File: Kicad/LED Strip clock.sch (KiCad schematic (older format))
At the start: 81 parts, among them J1 Conn_01x09_Male, J2 Conn_01x09_Male, J3 Conn_01x09_Male, J4 Conn_01x09_Male, J5 Conn_01x04_Male, J6 Barrel_Jack_Switch, U1 TPIC6B595, U10 5611BH, U11 5611BH, U12 5611BH, U13 MCP23008-xSO, U14 INA219AxDCN, U2 TPIC6B595, U3 TPIC6B595, U4 TPIC6B595, U5 74HCT244, U6 WeMos_D1_mini, U7 MAX809S, U8 L7805, U9 5611BH

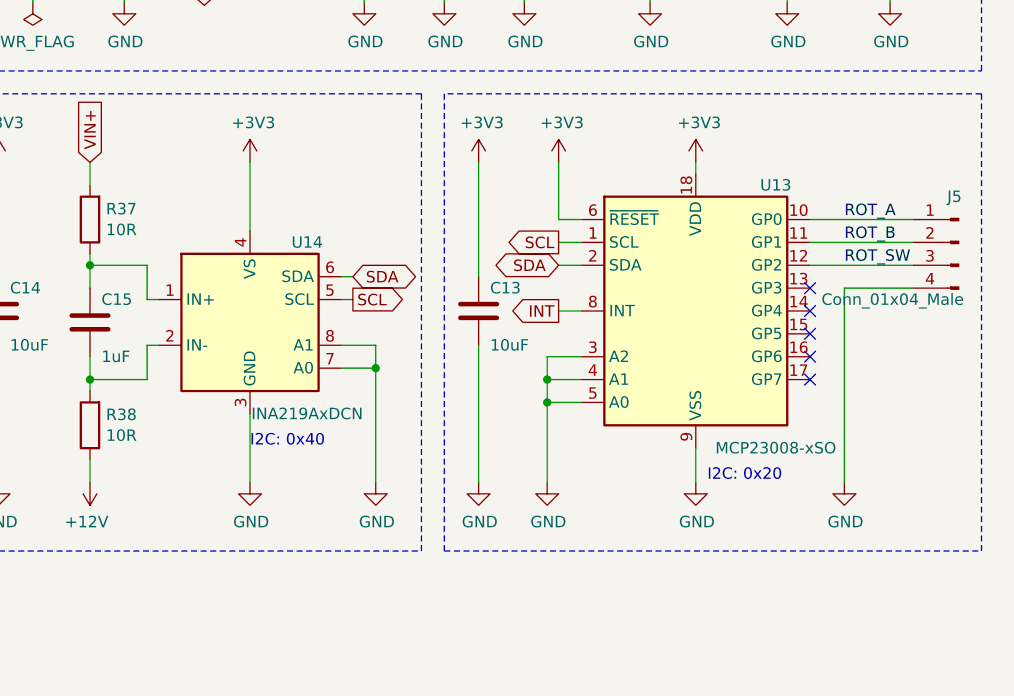
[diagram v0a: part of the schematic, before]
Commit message: Changed INA219AxDCN to INA219AxD.
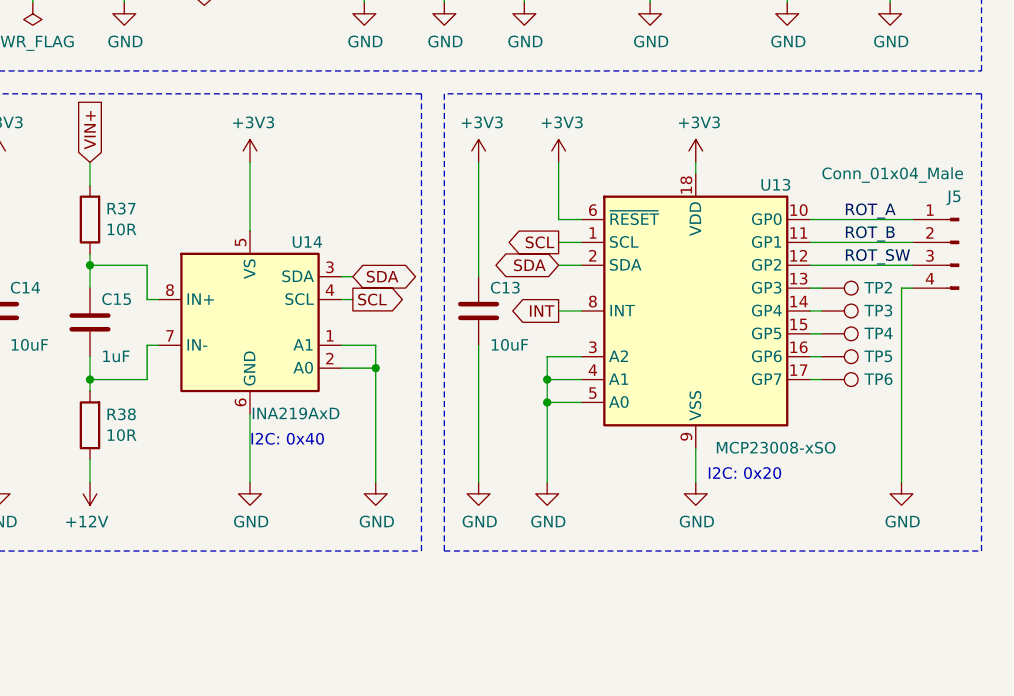
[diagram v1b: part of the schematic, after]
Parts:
- removed U14: INA219AxDCN, Package_TO_SOT_SMD:SOT-23-8, symbol Analog_ADC:INA219AxDCN
- added TP2, TP3, TP4, TP5, TP6: TestPoint, TestPoint:TestPoint_Pad_D1.0mm, symbol Connector:TestPoint
- added U14: INA219AxD, Package_SO:SOIC-8_3.9x4.9mm_P1.27mm, symbol Analog_ADC:INA219AxD
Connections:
- net +3V3: now also U14.5 (VS)
- net GND: now also U14.1 (A1), U14.2 (A0), U14.6 (GND)
- net SCL: now also U14.4 (SCL)
- net SDA: now also U14.3 (SDA)
- net at U13.13 (GP3): now also TP2.1
- net at U13.14 (GP4): now also TP3.1
- net at U13.15 (GP5): now also TP4.1
- net at U13.16 (GP6): now also TP5.1
- net at U13.17 (GP7): now also TP6.1
- net at C15.1, R37.1: now also U14.8 (IN+)
- net at C15.2, R38.2: now also U14.7 (IN-)
- no-connect marks 12 -> 7
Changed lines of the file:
@@
 Sheet 1 1
 Title "Driver for LED Strip clock"
-Date "2021-05-04"
+Date "2021-08-06"
 Rev "V1.0"
 Comp "https://github.com/atoomnetmarc/LED-Strip-clock"
@@
 P 11050 5100
 F 0 "J5" H 11100 5300 50  0000 R CNN
-F 1 "Conn_01x04_Male" H 11650 4850 50  0000 R CNN
+F 1 "Conn_01x04_Male" H 11650 5400 50  0000 R CNN
 F 2 "Connector_PinHeader_2.54mm:PinHeader_1x04_P2.54mm_Vertical" H 11050 5100 50  0001 C CNN
 F 3 "~" H 11050 5100 50  0001 C CNN
@@
 L power:GND #PWR038
 U 1 1 6093ED9B
-P 10550 6150
-F 0 "#PWR038" H 10550 5900 50  0001 C CNN
-F 1 "GND" H 10555 5977 50  0000 C CNN
-F 2 "" H 10550 6150 50  0001 C CNN
-F 3 "" H 10550 6150 50  0001 C CNN
-	1    10550 6150
+P 10800 6150
+F 0 "#PWR038" H 10800 5900 50  0001 C CNN
+F 1 "GND" H 10805 5977 50  0000 C CNN
+F 2 "" H 10800 6150 50  0001 C CNN
+F 3 "" H 10800 6150 50  0001 C CNN
+	1    10800 6150
 	1    0    0    -1
 $EndComp
@@
 ROT_SW
 Wire Wire Line
-	10550 5300 10550 6150
-Wire Wire Line
-	10550 5300 10850 5300
+	10800 5300 10800 6150
+Wire Wire Line
+	10800 5300 10850 5300
 Text Label 5250 3550 0    50   ~ 0
 ~OE_5V
@@
 Wire Wire Line
 	10400 5200 10850 5200
-NoConn ~ 10400 5300
-NoConn ~ 10400 5400
-NoConn ~ 10400 5500
-NoConn ~ 10400 5600
-NoConn ~ 10400 5700
 $Comp
 L power:GND #PWR060
@@
 Wire Notes Line
 	8700 6450 8700 4450
-$Comp
-L Analog_ADC:INA219AxDCN U14
-U 1 1 6147942B
-P 7950 5450
-F 0 "U14" H 8200 5800 50  0000 C CNN
-F 1 "INA219AxDCN" H 8200 5050 50  0000 C CNN
-F 2 "Package_TO_SOT_SMD:SOT-23-8" H 8600 5100 50  0001 C CNN
-F 3 "http://www.ti.com/lit/ds/symlink/ina219.pdf" H 8300 5350 50  0001 C CNN
-	1    7950 5450
-	1    0    0    -1
-$EndComp
 Text GLabel 8400 5250 2    50   BiDi ~ 0
 SDA
@@
 	-1   0    0    1
 $EndComp
+$Comp
+L Analog_ADC:INA219AxD U14
+U 1 1 610F2B75
+P 7950 5450
+F 0 "U14" H 8200 5800 50  0000 C CNN
+F 1 "INA219AxD" H 8150 5050 50  0000 C CNN
+F 2 "Package_SO:SOIC-8_3.9x4.9mm_P1.27mm" H 8750 5100 50  0001 C CNN
+F 3 "http://www.ti.com/lit/ds/symlink/ina219.pdf" H 8300 5350 50  0001 C CNN
+	1    7950 5450
+	1    0    0    -1
+$EndComp
+$Comp
+L Connector:TestPoint TP2
+U 1 1 611BBE01
+P 10450 5300
+F 0 "TP2" V 10450 5488 50  0000 L CNN
+F 1 "TestPoint" V 10495 5488 50  0001 L CNN
+F 2 "TestPoint:TestPoint_Pad_D1.0mm" H 10650 5300 50  0001 C CNN
+F 3 "~" H 10650 5300 50  0001 C CNN
+	1    10450 5300
+	0    1    1    0
+$EndComp
+$Comp
+L Connector:TestPoint TP3
+U 1 1 611BCA6F
+P 10450 5400
+F 0 "TP3" V 10450 5588 50  0000 L CNN
+F 1 "TestPoint" V 10495 5588 50  0001 L CNN
+F 2 "TestPoint:TestPoint_Pad_D1.0mm" H 10650 5400 50  0001 C CNN
+F 3 "~" H 10650 5400 50  0001 C CNN
+	1    10450 5400
+	0    1    1    0
+$EndComp
+$Comp
+L Connector:TestPoint TP4
+U 1 1 611BCC45
+P 10450 5500
+F 0 "TP4" V 10450 5688 50  0000 L CNN
+F 1 "TestPoint" V 10495 5688 50  0001 L CNN
+F 2 "TestPoint:TestPoint_Pad_D1.0mm" H 10650 5500 50  0001 C CNN
+F 3 "~" H 10650 5500 50  0001 C CNN
+	1    10450 5500
+	0    1    1    0
+$EndComp
+$Comp
+L Connector:TestPoint TP5
+U 1 1 611BCDDE
+P 10450 5600
+F 0 "TP5" V 10450 5788 50  0000 L CNN
+F 1 "TestPoint" V 10495 5788 50  0001 L CNN
+F 2 "TestPoint:TestPoint_Pad_D1.0mm" H 10650 5600 50  0001 C CNN
+F 3 "~" H 10650 5600 50  0001 C CNN
+	1    10450 5600
+	0    1    1    0
+$EndComp
+$Comp
+L Connector:TestPoint TP6
+U 1 1 611BCFF7
+P 10450 5700
+F 0 "TP6" V 10450 5888 50  0000 L CNN
+F 1 "TestPoint" V 10495 5888 50  0001 L CNN
+F 2 "TestPoint:TestPoint_Pad_D1.0mm" H 10650 5700 50  0001 C CNN
+F 3 "~" H 10650 5700 50  0001 C CNN
+	1    10450 5700
+	0    1    1    0
+$EndComp
+Wire Wire Line
+	10400 5300 10450 5300
+Wire Wire Line
+	10450 5400 10400 5400
+Wire Wire Line
+	10400 5500 10450 5500
+Wire Wire Line
+	10450 5600 10400 5600
+Wire Wire Line
+	10400 5700 10450 5700
 $EndSCHEMATC

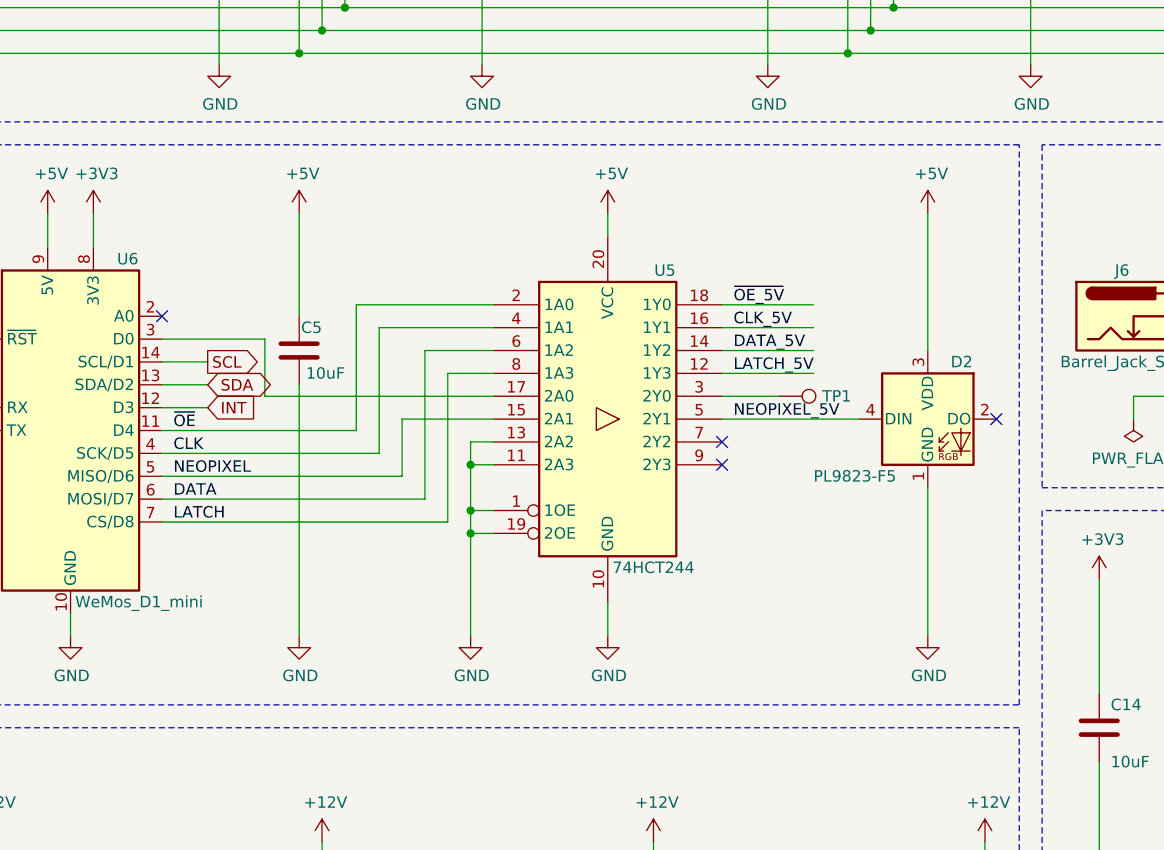
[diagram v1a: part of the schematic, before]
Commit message: Fixed power-on flash of digits.
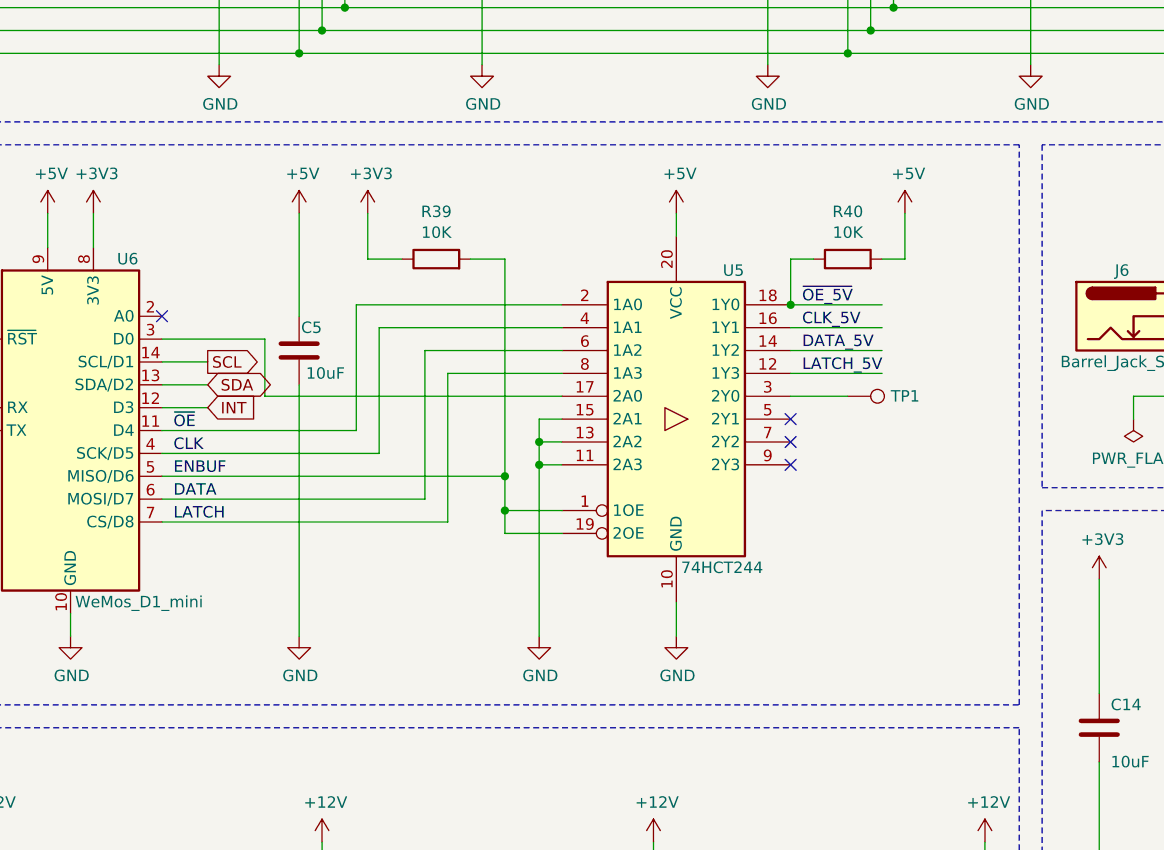
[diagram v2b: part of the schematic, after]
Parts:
- removed D2: PL9823-F5, LED_THT-extra:LED_D5.0mm-4_PL9823-F5, symbol LED-extra:PL9823-F5
- added R39, R40: 10K, Resistor_SMD:R_0805_2012Metric_Pad1.20x1.40mm_HandSolder, symbol Device:R
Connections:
- net +3V3: now also R39.1
- net +5V: now also R40.2
- net GND: now also U5.15 (2A1); no longer U5.1 (1OE), U5.19 (2OE)
- net ~OE_5V: now also R40.1
- net NEOPIXEL renamed ENBUF
- net ENBUF: now also U5.1 (1OE), U5.19 (2OE), R39.2; no longer U5.15 (2A1)
- net NEOPIXEL_5V: no longer names the net of U5.5 (2Y1)
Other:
- moved on the sheet: TP1, U5
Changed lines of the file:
@@
 Sheet 1 1
 Title "Driver for LED Strip clock"
-Date "2021-08-06"
+Date "2021-08-30"
 Rev "V1.0"
 Comp "https://github.com/atoomnetmarc/LED-Strip-clock"
@@
 L 74xx:74HCT244 U5
 U 1 1 608C7AB1
-P 4700 4050
-F 0 "U5" H 4950 4700 50  0000 C CNN
-F 1 "74HCT244" H 4900 3400 50  0000 C CNN
-F 2 "Package_DIP:DIP-20_W7.62mm_LongPads" H 4700 4050 50  0001 C CNN
-F 3 "https://assets.nexperia.com/documents/data-sheet/74HC_HCT244.pdf" H 4700 4050 50  0001 C CNN
-	1    4700 4050
+P 5000 4050
+F 0 "U5" H 5250 4700 50  0000 C CNN
+F 1 "74HCT244" H 5200 3400 50  0000 C CNN
+F 2 "Package_DIP:DIP-20_W7.62mm_LongPads" H 5000 4050 50  0001 C CNN
+F 3 "https://assets.nexperia.com/documents/data-sheet/74HC_HCT244.pdf" H 5000 4050 50  0001 C CNN
+	1    5000 4050
 	1    0    0    -1
 $EndComp
@@
 L power:GND #PWR041
 U 1 1 608CF759
-P 4700 5000
-F 0 "#PWR041" H 4700 4750 50  0001 C CNN
-F 1 "GND" H 4705 4827 50  0000 C CNN
-F 2 "" H 4700 5000 50  0001 C CNN
-F 3 "" H 4700 5000 50  0001 C CNN
-	1    4700 5000
+P 5000 5000
+F 0 "#PWR041" H 5000 4750 50  0001 C CNN
+F 1 "GND" H 5005 4827 50  0000 C CNN
+F 2 "" H 5000 5000 50  0001 C CNN
+F 3 "" H 5000 5000 50  0001 C CNN
+	1    5000 5000
 	1    0    0    -1
 $EndComp
@@
 L power:GND #PWR040
 U 1 1 608D1492
-P 4100 5000
-F 0 "#PWR040" H 4100 4750 50  0001 C CNN
-F 1 "GND" H 4105 4827 50  0000 C CNN
-F 2 "" H 4100 5000 50  0001 C CNN
-F 3 "" H 4100 5000 50  0001 C CNN
-	1    4100 5000
-	1    0    0    -1
-$EndComp
-Wire Wire Line
-	4200 4550 4100 4550
-Wire Wire Line
-	4100 4550 4100 5000
-Wire Wire Line
-	4200 4450 4100 4450
-Wire Wire Line
-	4100 4450 4100 4550
-Connection ~ 4100 4550
-Wire Wire Line
-	4700 4850 4700 5000
-Wire Wire Line
-	5200 3750 5600 3750
-Wire Wire Line
-	5200 3650 5600 3650
+P 4400 5000
+F 0 "#PWR040" H 4400 4750 50  0001 C CNN
+F 1 "GND" H 4405 4827 50  0000 C CNN
+F 2 "" H 4400 5000 50  0001 C CNN
+F 3 "" H 4400 5000 50  0001 C CNN
+	1    4400 5000
+	1    0    0    -1
+$EndComp
+Wire Wire Line
+	5000 4850 5000 5000
+Wire Wire Line
+	5500 3750 5900 3750
+Wire Wire Line
+	5500 3650 5900 3650
 $Comp
 L power:+5V #PWR031
 U 1 1 608D4D74
-P 4700 3150
-F 0 "#PWR031" H 4700 3000 50  0001 C CNN
-F 1 "+5V" H 4715 3323 50  0000 C CNN
-F 2 "" H 4700 3150 50  0001 C CNN
-F 3 "" H 4700 3150 50  0001 C CNN
-	1    4700 3150
-	1    0    0    -1
-$EndComp
-Wire Wire Line
-	4700 3250 4700 3150
-Wire Wire Line
-	5200 3850 5600 3850
-Wire Wire Line
-	5200 3550 5600 3550
-Wire Wire Line
-	4000 3850 4200 3850
-Wire Wire Line
-	3900 3750 4200 3750
-Wire Wire Line
-	3700 3650 4200 3650
-Wire Wire Line
-	3600 3550 4200 3550
+P 5000 3150
+F 0 "#PWR031" H 5000 3000 50  0001 C CNN
+F 1 "+5V" H 5015 3323 50  0000 C CNN
+F 2 "" H 5000 3150 50  0001 C CNN
+F 3 "" H 5000 3150 50  0001 C CNN
+	1    5000 3150
+	1    0    0    -1
+$EndComp
+Wire Wire Line
+	5000 3250 5000 3150
+Wire Wire Line
+	5500 3850 5900 3850
+Wire Wire Line
+	5500 3550 5900 3550
+Wire Wire Line
+	4000 3850 4500 3850
+Wire Wire Line
+	3900 3750 4500 3750
+Wire Wire Line
+	3700 3650 4500 3650
+Wire Wire Line
+	3600 3550 4500 3550
 $Comp
 L Connector:Conn_01x04_Male J5
@@
 Wire Wire Line
 	10800 5300 10850 5300
-Text Label 5250 3550 0    50   ~ 0
+Text Label 5550 3550 0    50   ~ 0
 ~OE_5V
-Text Label 5250 3850 0    50   ~ 0
+Text Label 5550 3850 0    50   ~ 0
 LATCH_5V
-Text Label 5250 3650 0    50   ~ 0
+Text Label 5550 3650 0    50   ~ 0
 CLK_5V
-Text Label 5250 3750 0    50   ~ 0
+Text Label 5550 3750 0    50   ~ 0
 DATA_5V
 $Comp
@@
 Wire Wire Line
 	3600 3550 3600 4100
-NoConn ~ 5200 4150
-NoConn ~ 5200 4250
-Wire Wire Line
-	4100 4450 4100 4250
-Wire Wire Line
-	4100 4250 4200 4250
-Connection ~ 4100 4450
-Wire Wire Line
-	4100 4250 4100 4150
-Wire Wire Line
-	4100 4150 4200 4150
-Connection ~ 4100 4250
+NoConn ~ 5500 4150
+NoConn ~ 5500 4250
+Wire Wire Line
+	4400 4250 4500 4250
+Wire Wire Line
+	4400 4250 4400 4150
+Wire Wire Line
+	4400 4150 4500 4150
+Connection ~ 4400 4250
 Wire Wire Line
 	10750 3500 10750 3150
@@
 $EndComp
 Wire Wire Line
-	3800 4300 3800 4050
-Wire Wire Line
-	3800 4050 4200 4050
-Wire Wire Line
-	4200 3950 3200 3950
+	4500 3950 3200 3950
 Wire Wire Line
 	3200 3950 3200 3700
@@
 L Connector:TestPoint TP1
 U 1 1 611FE123
-P 5450 3950
-F 0 "TP1" V 5450 4138 50  0000 L CNN
-F 1 "TestPoint" V 5495 4138 50  0001 L CNN
-F 2 "TestPoint:TestPoint_THTPad_D1.5mm_Drill0.7mm" H 5650 3950 50  0001 C CNN
-F 3 "~" H 5650 3950 50  0001 C CNN
-	1    5450 3950
-	0    1    1    0
-$EndComp
-Wire Wire Line
-	5200 3950 5450 3950
-$Comp
-L LED-extra:PL9823-F5 D2
-U 1 1 61220BB0
-P 6100 4050
-F 0 "D2" H 6200 4300 50  0000 L CNN
-F 1 "PL9823-F5" H 5600 3800 50  0000 L CNN
-F 2 "LED_THT-extra:LED_D5.0mm-4_PL9823-F5" H 6150 3750 50  0001 L TNN
-F 3 "" H 6200 3675 50  0001 L TNN
-	1    6100 4050
-	1    0    0    -1
-$EndComp
-$Comp
-L power:GND #PWR054
-U 1 1 6122258F
-P 6100 5000
-F 0 "#PWR054" H 6100 4750 50  0001 C CNN
-F 1 "GND" H 6105 4827 50  0000 C CNN
-F 2 "" H 6100 5000 50  0001 C CNN
-F 3 "" H 6100 5000 50  0001 C CNN
-	1    6100 5000
-	1    0    0    -1
-$EndComp
-$Comp
-L power:+5V #PWR053
-U 1 1 61222901
-P 6100 3150
-F 0 "#PWR053" H 6100 3000 50  0001 C CNN
-F 1 "+5V" H 6115 3323 50  0000 C CNN
-F 2 "" H 6100 3150 50  0001 C CNN
-F 3 "" H 6100 3150 50  0001 C CNN
-	1    6100 3150
-	1    0    0    -1
-$EndComp
-Wire Wire Line
-	6100 3750 6100 3150
-Wire Wire Line
-	6100 5000 6100 4350
-Wire Wire Line
-	5200 4050 5800 4050
-NoConn ~ 6400 4050
-Text Label 5250 4050 0    50   ~ 0
-NEOPIXEL_5V
+P 5750 3950
+F 0 "TP1" V 5750 4138 50  0000 L CNN
+F 1 "TestPoint" V 5795 4138 50  0001 L CNN
+F 2 "TestPoint:TestPoint_THTPad_D1.5mm_Drill0.7mm" H 5950 3950 50  0001 C CNN
+F 3 "~" H 5950 3950 50  0001 C CNN
+	1    5750 3950
+	0    1    1    0
+$EndComp
+Wire Wire Line
+	5500 3950 5750 3950
 Text GLabel 2950 4000 2    50   Input ~ 0
 INT
@@
 Text GLabel 2950 3800 2    50   Output ~ 0
 SCL
-Text Label 2800 4300 0    50   ~ 0
-NEOPIXEL
 Wire Wire Line
 	3200 3700 2750 3700
@@
 	1    0    0    -1
 $EndComp
-Wire Wire Line
-	2750 4300 3800 4300
 $Comp
 L power:+3V3 #PWR027
@@
 Wire Wire Line
 	10400 5700 10450 5700
+NoConn ~ 5500 4050
+Wire Wire Line
+	4400 4150 4400 4050
+Wire Wire Line
+	4400 4050 4500 4050
+Connection ~ 4400 4150
+Wire Wire Line
+	4400 4250 4400 5000
+Wire Wire Line
+	4500 4550 4250 4550
+Wire Wire Line
+	4250 4550 4250 4450
+Wire Wire Line
+	4250 4300 2750 4300
+Wire Wire Line
+	4500 4450 4250 4450
+Connection ~ 4250 4450
+Wire Wire Line
+	4250 4450 4250 4300
+$Comp
+L Device:R R39
+U 1 1 61392FE4
+P 3950 3350
+F 0 "R39" V 4157 3350 50  0000 C CNN
+F 1 "10K" V 4066 3350 50  0000 C CNN
+F 2 "Resistor_SMD:R_0805_2012Metric_Pad1.20x1.40mm_HandSolder" V 3880 3350 50  0001 C CNN
+F 3 "~" H 3950 3350 50  0001 C CNN
+	1    3950 3350
+	0    -1   -1   0
+$EndComp
+Wire Wire Line
+	4250 4300 4250 3350
+Wire Wire Line
+	4250 3350 4100 3350
+Connection ~ 4250 4300
+Wire Wire Line
+	3800 3350 3650 3350
+Wire Wire Line
+	3650 3350 3650 3150
+$Comp
+L power:+3V3 #PWR053
+U 1 1 613D3F74
+P 3650 3150
+F 0 "#PWR053" H 3650 3000 50  0001 C CNN
+F 1 "+3V3" H 3665 3323 50  0000 C CNN
+F 2 "" H 3650 3150 50  0001 C CNN
+F 3 "" H 3650 3150 50  0001 C CNN
+	1    3650 3150
+	1    0    0    -1
+$EndComp
+Text Label 2800 4300 0    50   ~ 0
+ENBUF
+$Comp
+L Device:R R40
+U 1 1 613D6083
+P 5750 3350
+F 0 "R40" V 5957 3350 50  0000 C CNN
+F 1 "10K" V 5866 3350 50  0000 C CNN
+F 2 "Resistor_SMD:R_0805_2012Metric_Pad1.20x1.40mm_HandSolder" V 5680 3350 50  0001 C CNN
+F 3 "~" H 5750 3350 50  0001 C CNN
+	1    5750 3350
+	0    -1   -1   0
+$EndComp
+$Comp
+L power:+5V #PWR054
+U 1 1 613D6CC8
+P 6000 3150
+F 0 "#PWR054" H 6000 3000 50  0001 C CNN
+F 1 "+5V" H 6015 3323 50  0000 C CNN
+F 2 "" H 6000 3150 50  0001 C CNN
+F 3 "" H 6000 3150 50  0001 C CNN
+	1    6000 3150
+	1    0    0    -1
+$EndComp
+Wire Wire Line
+	5600 3350 5500 3350
+Wire Wire Line
+	5500 3350 5500 3550
+Connection ~ 5500 3550
+Wire Wire Line
+	5900 3350 6000 3350
+Wire Wire Line
+	6000 3350 6000 3150
 $EndSCHEMATC
